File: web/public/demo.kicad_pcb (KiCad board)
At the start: 2 copper layers, 50 x 30 mm, 1 part

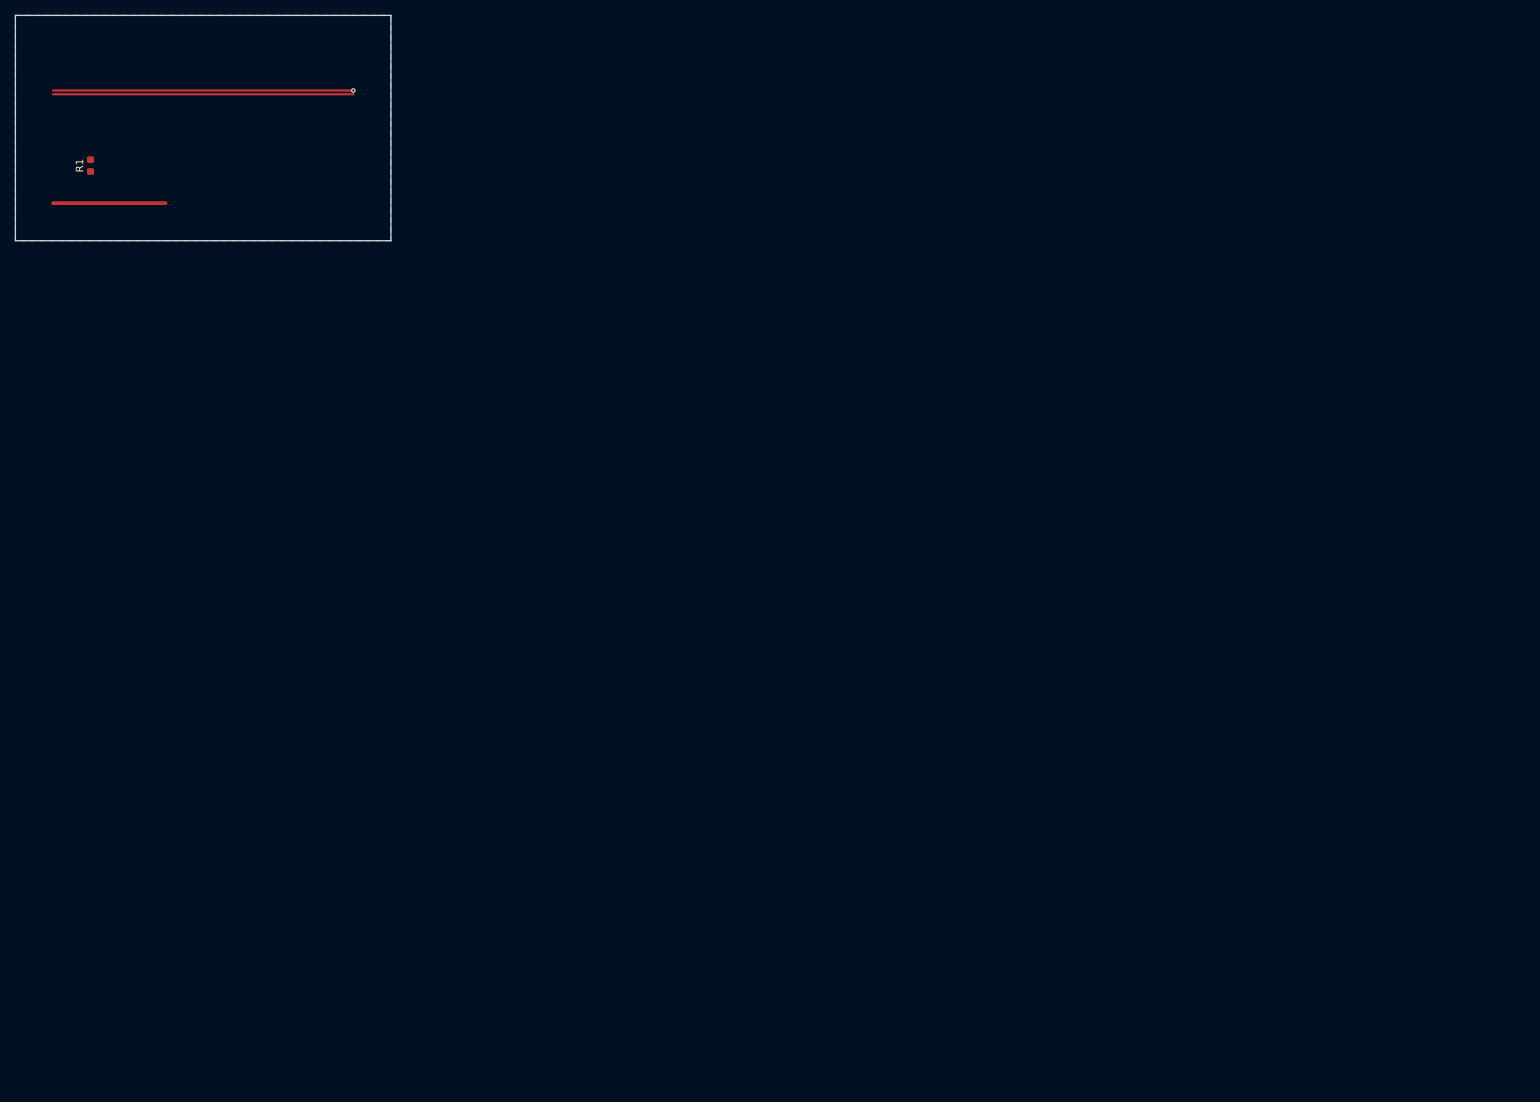
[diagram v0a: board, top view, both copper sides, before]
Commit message: The demo board is now a real converter: LibreSolar MPPT 2420 HC
The served demo was a 2 kB synthetic two-trace board — it demonstrated
coupled-run and nothing Faraday is actually FOR. It is now the
LibreSolar MPPT 2420 HC (CERN-OHL-W-2.0, already attributed in
fixtures/real/ATTRIBUTION.md): a real 20 A synchronous buck that shows
switch nodes, the DERIVED commutation loop (Q1+Q2+C3 by
current-switching analysis), the assumed-stackup flow (KiCad 5 file,
no stackup), return-path breaks, the near-field map and the emissions
panel. The chip names it and carries the license in its tooltip.

The old tiny board still had a job — the stitching fix's
honest-refusal path (no reference via to copy a style from) — so it
moved inline into the returnpath spec instead of being served.

Co-Authored-By: Claude Opus 5 (1M context) <noreply@anthropic.com>
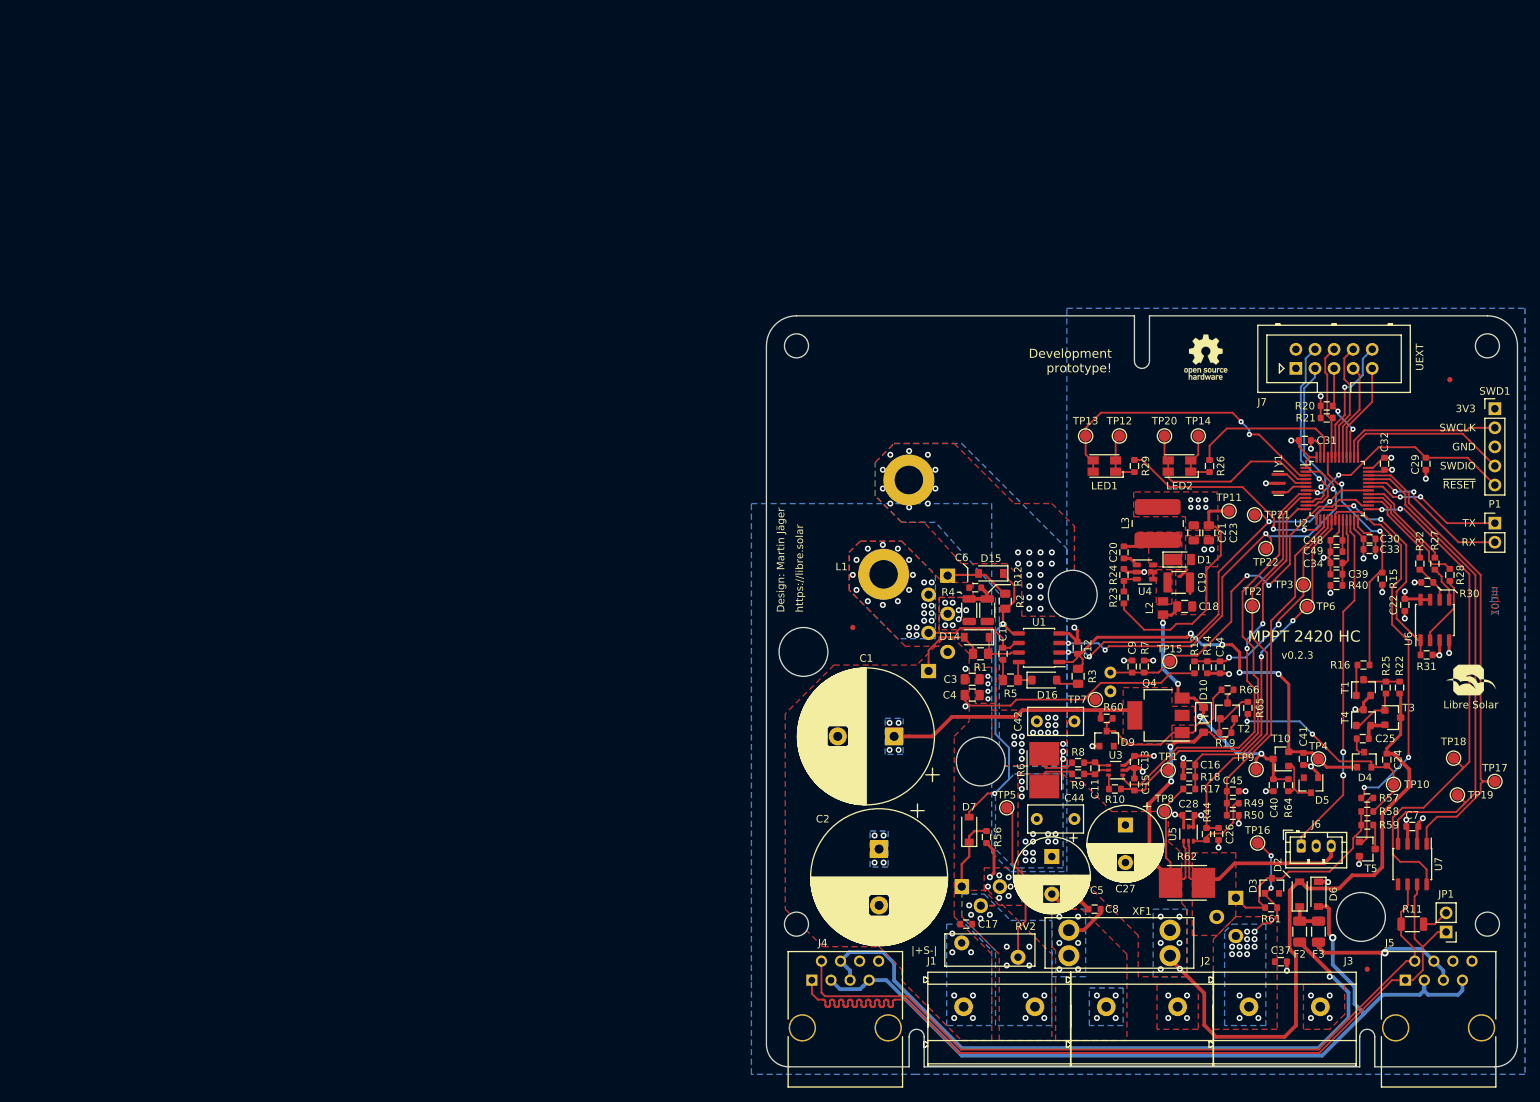
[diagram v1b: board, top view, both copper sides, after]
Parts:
- added C1: 390µF, Capacitor_THT:CP_Radial_D18.0mm_P7.50mm, F.Cu at (117.0, 96.0)
- added C10: 100nF, LibreSolar:C_0603_1608, F.Cu at (131.5, 85.0)
- added C11: 1nF, LibreSolar:C_0603_1608, F.Cu at (143.8, 100.2)
- added C12: 2.2µF, LibreSolar:C_0603_1608, F.Cu at (141.4, 84.2)
- added C13: 100nF, LibreSolar:C_0603_1608, F.Cu at (149.0, 99.4)
- added C14: 10nF, LibreSolar:C_0603_1608, F.Cu at (160.4, 86.8)
- added C15: 1nF, LibreSolar:C_0603_1608, F.Cu at (149.0, 102.4)
- added C16: 10nF, LibreSolar:C_0603_1608, F.Cu at (156.3, 99.8)
- added C17: 10nF, LibreSolar:C_0603_1608, F.Cu at (126.6, 121.0)
- added C18: 1µF, LibreSolar:C_0805_2012, F.Cu at (155.7, 78.7)
- added C19: 4.7µF, LibreSolar:C_1210_3225, F.Cu at (154.9, 75.5)
- added C2: 390µF, Capacitor_THT:CP_Radial_D18.0mm_P7.50mm, F.Cu at (115.0, 111.0)
- added C20: 100nF, LibreSolar:C_0603_1608, F.Cu at (147.6, 71.5)
- added C21: 10µF, LibreSolar:C_0805_2012, F.Cu at (156.9, 68.9)
- added C22: 100nF, LibreSolar:C_0603_1608, F.Cu at (185.0, 78.5)
- added C23: 10µF, LibreSolar:C_0805_2012, F.Cu at (158.9, 68.9)
- added C24: 100nF, LibreSolar:C_0603_1608, F.Cu at (182.6, 99.1)
- added C25: 10nF, LibreSolar:C_0603_1608, F.Cu at (179.4, 96.3)
- added C26: 10nF, LibreSolar:C_0603_1608, F.Cu at (160.2, 109.0)
- added C27: 680µF, Capacitor_THT:CP_Radial_D10.0mm_P5.00mm, F.Cu at (147.8, 107.8)
- added C28: 100nF, LibreSolar:C_0603_1608, F.Cu at (156.2, 106.5)
- added C29: 100nF, LibreSolar:C_0603_1608, F.Cu at (187.8, 59.7)
- added C3: 1µF, LibreSolar:C_0805_2012, F.Cu at (127.4, 88.4)
- added C30: 100nF, LibreSolar:C_0603_1608, F.Cu at (180.3, 69.7)
- added C31: 100nF, LibreSolar:C_0603_1608, F.Cu at (171.7, 56.6)
- added C32: 100nF, LibreSolar:C_0603_1608, F.Cu at (182.3, 59.7)
- added C33: 2.2µF, LibreSolar:C_0603_1608, F.Cu at (180.3, 71.1)
- added C34: 10nF, LibreSolar:C_0603_1608, F.Cu at (175.9, 72.9)
- added C37: 10nF, LibreSolar:C_0603_1608, F.Cu at (168.5, 126.0)
- added C39: 2.2µF, LibreSolar:C_0603_1608, F.Cu at (175.9, 74.4)
- added C4: 100nF, LibreSolar:C_0805_2012, F.Cu at (127.4, 90.5)
- added C40: 1µF, LibreSolar:C_0603_1608, F.Cu at (167.5, 102.5)
- added C41: 4.7µF, LibreSolar:C_0603_1608, F.Cu at (171.5, 99.0)
- added C42: 0.22µF, Capacitor_THT:C_Rect_L7.2mm_W3.5mm_P5.00mm_FKS2_FKP2_MKS2_MKP2, F.Cu at (136.0, 94.0)
- added C44: 0.22µF, Capacitor_THT:C_Rect_L7.2mm_W3.5mm_P5.00mm_FKS2_FKP2_MKS2_MKP2, F.Cu at (141.0, 107.0)
- added C45: 10nF, LibreSolar:C_0603_1608, F.Cu at (162.1, 103.3)
- added C48: 100nF, LibreSolar:C_0603_1608, F.Cu at (175.9, 69.9)
- added C49: 2.2µF, LibreSolar:C_0603_1608, F.Cu at (175.9, 71.4)
- added C5: 680µF, Capacitor_THT:CP_Radial_D10.0mm_P5.00mm, F.Cu at (138.0, 112.0)
- added C6: 2.2nF, LibreSolar:C_0603_1608, F.Cu at (127.8, 76.2)
- added C7: 100nF, LibreSolar:C_0603_1608, F.Cu at (186.0, 108.0)
- added C8: 10nF, LibreSolar:C_0603_1608, F.Cu at (143.7, 119.0)
- added C9: 100nF, LibreSolar:C_0603_1608, F.Cu at (148.7, 86.7)
- added D1: SS16FP, Diode_SMD:D_PowerDI-123, F.Cu at (155.0, 72.5)
- added D10: 1N4148, LibreSolar:D_SOD-123, F.Cu at (158.2, 93.8)
- added D14: SS14FL, Diode_SMD:D_SOD-123, F.Cu at (128.0, 82.8)
- added D15: SS14FL, Diode_SMD:D_SOD-123, F.Cu at (129.9, 74.3)
- added D16: 1N4148, LibreSolar:D_SOD-123, F.Cu at (137.0, 88.5)
- added D2: NRVTS260ESFT1G, Diode_SMD:D_SOD-123, F.Cu at (171.0, 117.0)
- added D3: 12V, Diode_SMD:D_SOT-23_ANK, F.Cu at (167.3, 115.9)
- added D4: BAS70-04, Package_TO_SOT_SMD:SOT-23, F.Cu at (179.6, 99.1)
- added D5: 12V, Diode_SMD:D_SOT-23_ANK, F.Cu at (172.5, 102.5)
- added D6: NRVTS260ESFT1G, Diode_SMD:D_SOD-123, F.Cu at (173.5, 117.0)
- added D7: SS14FL, Diode_SMD:D_SOD-123, F.Cu at (127.0, 108.4)
- added D9: 47V, Diode_SMD:D_SOT-23_ANK, F.Cu at (145.3, 96.3)
- added F1: 25A, LibreSolar:NULL, F.Cu at (147.0, 123.5)
- added F2: 500mA, Fuse:Fuse_1206_3216Metric, F.Cu at (171.0, 122.0)
- added F3: 500mA, Fuse:Fuse_1206_3216Metric, F.Cu at (173.5, 122.0)
- added FID1: Fiducial, LibreSolar:Fiducial_0.7mm, F.Cu at (180.0, 127.0)
- added FID2: Fiducial, LibreSolar:Fiducial_0.7mm, F.Cu at (111.5, 81.5)
- added FID3: Fiducial, LibreSolar:Fiducial_0.7mm, F.Cu at (191.0, 48.5)
- added J1: MKDS 5/ 2-9,5, LibreSolar:Phoenix_Contact_MKDS_5-2-9,5, F.Cu at (126.2, 132.0)
- added J2: MKDS 5/ 2-9,5, LibreSolar:Phoenix_Contact_MKDS_5-2-9,5, F.Cu at (145.2, 132.0)
- added J3: MKDS 5/ 2-9,5, LibreSolar:Phoenix_Contact_MKDS_5-2-9,5, F.Cu at (164.2, 132.0)
- added J4: 8P8C, LibreSolar:RJ45_8P8C, F.Cu at (110.5, 131.0)
- added J5: 8P8C, LibreSolar:RJ45_8P8C, F.Cu at (189.5, 131.0)
- added J6: JST PH, Connector_JST:JST_PH_B3B-PH-K_1x03_P2.00mm_Vertical, F.Cu at (171.2, 110.6)
- added J7: UEXT, LibreSolar:Box_Header_2x05x2.54mm_Straight, F.Cu at (170.5, 47.0)
- added JP1: Jumper_NC_Small, Connector_PinHeader_2.54mm:PinHeader_1x02_P2.54mm_Vertical, F.Cu at (190.5, 122.0)
- added L1: 53µH, LibreSolar:Inductor_Toroid_D32.8mm_4mm2, F.Cu at (120.0, 58.0)
- added L2: 4.7µH, Inductor_SMD:L_0805_2012Metric, F.Cu at (152.8, 78.9)
- added L3: 47µH, LibreSolar:Bourns_SRN6045TA, F.Cu at (152.1, 67.7)
- added LED1: LED_Dual_PLCC4, LED_SMD:LED_Avago_PLCC4_3.2x2.8mm_CW, F.Cu at (145.0, 60.0)
- added LED2: LED_Dual_PLCC4, LED_SMD:LED_Avago_PLCC4_3.2x2.8mm_CW, F.Cu at (155.0, 60.0)
- added LOGO1: LIBRE_SOLAR, LibreSolar:LIBRESOLAR_LOGO, F.Cu at (191.5, 90.5)
- added LOGO2: OPEN_HARDWARE, Symbol:OSHW-Logo_5.7x6mm_SilkScreen, F.Cu at (158.5, 45.5)
- added MK1: Mounting_Hole, MountingHole:MountingHole_3.2mm_M3, F.Cu at (104.0, 121.0)
- added MK2: Mounting_Hole, MountingHole:MountingHole_3.2mm_M3, F.Cu at (196.0, 121.0)
- added MK3: Mounting_Hole, MountingHole:MountingHole_3.2mm_M3, F.Cu at (196.0, 44.0)
- added MK4: Mounting_Hole, MountingHole:MountingHole_3.2mm_M3, F.Cu at (104.0, 44.0)
- added P1: CONN_01X02, Connector_PinHeader_2.54mm:PinHeader_1x02_P2.54mm_Vertical, F.Cu at (197.0, 67.6)
- added Q1: IPA045N10N3G, LibreSolar:TO-220-3_Horizontal_BottomHeatsink, B.Cu at (121.6, 87.3)
- added Q2: IPA045N10N3G, LibreSolar:TO-220-3_Horizontal_BottomHeatsink, B.Cu at (124.1, 74.6)
- added Q3: IPA045N10N3G, LibreSolar:TO-220-3_Horizontal_BottomHeatsink, B.Cu at (126.0, 116.0)
- added Q4: BUK98180-100A, Package_TO_SOT_SMD:SOT-223-3_TabPin2, F.Cu at (152.2, 93.2)
- added Q7: IPA045N10N3G, LibreSolar:TO-220-3_Horizontal_BottomHeatsink, B.Cu at (162.5, 117.5)
- added R10: 1k, LibreSolar:R_0603_1608, F.Cu at (146.4, 103.0)
- added R11: 120R, LibreSolar:R_1206_3216, F.Cu at (186.0, 121.0)
- added R12: 4R7, LibreSolar:R_1206_3216, F.Cu at (129.4, 79.2)
- added R13: 100k, LibreSolar:R_0603_1608, F.Cu at (157.0, 86.8)
- added R14: 2.2k, LibreSolar:R_0603_1608, F.Cu at (158.7, 86.8)
- added R15: 1M, LibreSolar:R_0603_1608, F.Cu at (182.0, 75.0)
- added R16: 10k, LibreSolar:R_0603_1608, F.Cu at (179.5, 86.5)
- added R17: 100k, LibreSolar:R_0603_1608, F.Cu at (156.3, 103.0)
- added R18: 5.6k, LibreSolar:R_0603_1608, F.Cu at (156.3, 101.4)
- added R19: 10k, LibreSolar:R_0603_1608, F.Cu at (161.1, 95.5)
- added R2: 3R3, LibreSolar:R_0805_2012, F.Cu at (131.8, 78.0)
- added R20: 2.2k, LibreSolar:R_0603_1608, F.Cu at (174.6, 52.0)
- added R21: 2.2k, LibreSolar:R_0603_1608, F.Cu at (174.6, 53.6)
- added R22: 100k, LibreSolar:R_0603_1608, F.Cu at (184.3, 89.5)
- added R23: 33k, LibreSolar:R_0603_1608, F.Cu at (147.6, 77.5)
- added R24: 10k, LibreSolar:R_0603_1608, F.Cu at (147.6, 74.5)
- added R25: 1k, LibreSolar:R_0603_1608, F.Cu at (182.5, 89.5)
- added R26: 1k, LibreSolar:R_0603_1608, F.Cu at (159.0, 60.0)
- added R27: 47R, LibreSolar:R_0603_1608, F.Cu at (189.0, 73.0)
- added R28: 47R, LibreSolar:R_0603_1608, F.Cu at (191.0, 74.5)
- added R29: 1k, LibreSolar:R_0603_1608, F.Cu at (149.0, 60.0)
- added R3: 3R3, LibreSolar:R_0805_2012, F.Cu at (141.5, 88.0)
- added R30: 100k, LibreSolar:R_0603_1608, F.Cu at (188.0, 75.5)
- added R31: 2.2k, LibreSolar:R_0603_1608, F.Cu at (187.9, 85.2)
- added R32: 47R, LibreSolar:R_0603_1608, F.Cu at (187.0, 73.0)
- added R4: 4R7, LibreSolar:R_1206_3216, F.Cu at (127.0, 79.2)
- added R40: 47R, LibreSolar:R_0603_1608, F.Cu at (175.9, 75.9)
- added R44: 2.2k, LibreSolar:R_0603_1608, F.Cu at (158.6, 109.0)
- added R49: 10k, LibreSolar:R_0603_1608, F.Cu at (162.1, 104.9)
- added R5: 3R3, LibreSolar:R_0805_2012, F.Cu at (132.5, 88.5)
- added R50: 8.2k, LibreSolar:C_0603_1608, F.Cu at (162.1, 106.5)
- added R56: 1M, LibreSolar:R_0603_1608, F.Cu at (129.3, 109.4)
- added R57: 2.2k, LibreSolar:R_0603_1608, F.Cu at (180.0, 104.2)
- added R58: 100k, LibreSolar:R_0603_1608, F.Cu at (180.0, 106.0)
- added R59: 10k, LibreSolar:R_0603_1608, F.Cu at (180.0, 107.8)
- added R6: 2m, LibreSolar:R_Bourns_CRE2512, F.Cu at (137.0, 100.5)
- added R60: 100k, LibreSolar:R_0603_1608, F.Cu at (145.3, 93.6)
- added R61: 1M, LibreSolar:R_0603_1608, F.Cu at (167.2, 118.8)
- added R62: 2m, LibreSolar:R_Bourns_CRE2512, F.Cu at (156.0, 115.5)
- added R64: 10k, LibreSolar:R_0603_1608, F.Cu at (169.5, 102.5)
- added R65: 100k, LibreSolar:R_0603_1608, F.Cu at (164.1, 92.2)
- added R66: 1k, LibreSolar:R_0603_1608, F.Cu at (161.4, 89.8)
- added R7: 10k, LibreSolar:R_0603_1608, F.Cu at (150.3, 86.7)
- added R8: 10R, LibreSolar:R_0603_1608, F.Cu at (141.5, 99.5)
- added R9: 10R, LibreSolar:R_0603_1608, F.Cu at (141.5, 101.0)
- added RT1: 10k, Capacitor_THT:C_Disc_D3.8mm_W2.6mm_P2.50mm, B.Cu at (145.8, 87.5)
- added RV2: 82V, Varistor:RV_Disc_D12mm_W4.3mm_P7.5mm, F.Cu at (126.0, 123.5)
- added SWD1: ST_Nucleo_SWD, Connector_PinHeader_2.54mm:PinHeader_1x05_P2.54mm_Vertical, F.Cu at (197.0, 52.4)
- added T1: BC846B, LibreSolar:SOT-23, F.Cu at (179.5, 89.5)
- added T10: BC846B, LibreSolar:SOT-23, F.Cu at (168.5, 99.0)
- added T2: BC846B, LibreSolar:SOT-23, F.Cu at (161.4, 92.6)
- added T3: BC846B, LibreSolar:SOT-23, F.Cu at (183.4, 93.5)
- added T4: BC856B, LibreSolar:SOT-23, F.Cu at (179.5, 93.5)
- added T5: BC846B, LibreSolar:SOT-23, F.Cu at (180.0, 111.0)
- added TP1: 1.5mm, TestPoint:TestPoint_Pad_D1.5mm, F.Cu at (153.5, 100.5)
- added TP10: 1.5mm, TestPoint:TestPoint_Pad_D1.5mm, F.Cu at (183.5, 102.4)
- added TP11: 1.5mm, TestPoint:TestPoint_Pad_D1.5mm, F.Cu at (161.6, 66.0)
- added TP12: 1.5mm, TestPoint:TestPoint_Pad_D1.5mm, F.Cu at (147.0, 56.0)
- added TP13: 1.5mm, TestPoint:TestPoint_Pad_D1.5mm, F.Cu at (142.5, 56.0)
- added TP14: 1.5mm, TestPoint:TestPoint_Pad_D1.5mm, F.Cu at (157.5, 56.0)
- added TP15: 1.5mm, TestPoint:TestPoint_Pad_D1.5mm, F.Cu at (153.7, 86.0)
- added TP16: 1.5mm, TestPoint:TestPoint_Pad_D1.5mm, F.Cu at (165.4, 110.2)
- added TP17: 1.5mm, TestPoint:TestPoint_Pad_D1.5mm, F.Cu at (197.0, 102.0)
- added TP18: 1.5mm, TestPoint:TestPoint_Pad_D1.5mm, F.Cu at (191.5, 98.9)
- added TP19: 1.5mm, TestPoint:TestPoint_Pad_D1.5mm, F.Cu at (192.0, 103.8)
- added TP2: 1.5mm, TestPoint:TestPoint_Pad_D1.5mm, F.Cu at (164.7, 78.6)
- added TP20: 1.5mm, TestPoint:TestPoint_Pad_D1.5mm, F.Cu at (153.0, 56.0)
- added TP21: 1.5mm, TestPoint:TestPoint_Pad_D1.5mm, F.Cu at (165.0, 66.5)
- added TP22: 1.5mm, TestPoint:TestPoint_Pad_D1.5mm, F.Cu at (166.5, 71.0)
- added TP3: 1.5mm, TestPoint:TestPoint_Pad_D1.5mm, F.Cu at (171.5, 75.8)
- added TP4: 1.5mm, TestPoint:TestPoint_Pad_D1.5mm, F.Cu at (173.5, 99.0)
- added TP5: 1.5mm, TestPoint:TestPoint_Pad_D1.5mm, F.Cu at (132.0, 105.5)
- added TP6: 1.5mm, TestPoint:TestPoint_Pad_D1.5mm, F.Cu at (172.0, 78.7)
- added TP7: 1.5mm, TestPoint:TestPoint_Pad_D1.5mm, F.Cu at (143.8, 91.1)
- added TP8: 1.5mm, TestPoint:TestPoint_Pad_D1.5mm, F.Cu at (153.0, 106.0)
- added TP9: 1.5mm, TestPoint:TestPoint_Pad_D1.5mm, F.Cu at (165.2, 100.4)
- added U1: LM5107, LibreSolar:SOIC-8_3.9x4.9mm_Pitch1.27mm, F.Cu at (136.3, 84.2)
- added U2: STM32G431CBTx, Package_QFP:LQFP-48_7x7mm_P0.5mm, F.Cu at (176.0, 63.0)
- added U3: INA186, Package_TO_SOT_SMD:SOT-363_SC-70-6, F.Cu at (146.5, 100.5)
- added U4: LMR16006X, LibreSolar:SOT-23-6, F.Cu at (150.4, 74.1)
- added U5: INA186, Package_TO_SOT_SMD:SOT-363_SC-70-6, F.Cu at (156.2, 109.0)
- added U6: W25Q80DVS, LibreSolar:SOIC-8_3.9x4.9mm_Pitch1.27mm, F.Cu at (189.0, 80.5)
- added U7: TCAN334, LibreSolar:SOIC-8_3.9x4.9mm_Pitch1.27mm, F.Cu at (186.0, 113.0)
- added XF1: Fuse_Holder, LibreSolar:Keystone-Fuse-3557-2, F.Cu at (147.0, 123.5)
- added Y1: 8MHz, LibreSolar:Resonator_Murata_CSTNE, F.Cu at (168.2, 62.3)
- R1: value 100n -> 3R3; footprint Resistor_SMD:R_0603_1608Metric -> LibreSolar:R_0805_2012
- moved R1 135.2 mm to (128.5, 85.0), turned to 0 degrees
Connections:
- R1 pad 1: CLK -> Net-(D14-Pad2)
- R1 pad 2: GND -> /DC/DC/HS_DRV
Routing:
- net VBUS: track 0.00 -> 142.2 mm, vias 0 -> 22
- net /CAN_H: track 0.00 -> 118.8 mm
- net /CAN_GND: track 0.00 -> 114.9 mm, vias 0 -> 1
- net /CAN_L: track 0.00 -> 102.6 mm
- net /CAN/CAN_PWR1: track 0.00 -> 92.6 mm, vias 0 -> 1
- net +3V3: track 0.00 -> 71.5 mm, vias 0 -> 17
- net /DCDC_HV+: track 0.00 -> 69.7 mm, vias 0 -> 17
- net /CAN/CAN_STB: track 0.00 -> 69.7 mm, vias 0 -> 2
- net GND: track 15.0 -> 82.7 mm, vias 0 -> 64
- net /CAN/CAN_RX: track 0.00 -> 66.1 mm
- net /CAN/CAN_TX: track 0.00 -> 63.3 mm
- net /MCU/ADC12_IN1: track 0.00 -> 59.2 mm
- net /DC/DC/PWM_LS: track 0.00 -> 58.7 mm, vias 0 -> 4
- net +12V: track 0.00 -> 58.4 mm, vias 0 -> 4
- net /DC/DC/PWM_HS: track 0.00 -> 56.3 mm, vias 0 -> 4
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- added copper zone on 3V3, net +3V3
- added copper zone on F.Cu, net +3V3
- added copper zone on B.Cu, net /BAT+
- added copper zone on F.Cu, net /BAT+
- added copper zone on 3V3, net /DC/DC/SHUNT_DCDC_P
- added copper zone on B.Cu, net /DC/DC/SHUNT_DCDC_P
- added copper zone on F.Cu, net /DC/DC/SHUNT_DCDC_P
- added copper zone on 3V3, net /DC/DC/SW_NODE
- added copper zone on B.Cu, net /DC/DC/SW_NODE
- added copper zone on F.Cu, net /DC/DC/SW_NODE
- added copper zone on GND, net /DC/DC/SW_NODE
- added copper zone on 3V3, net /DCDC_HV+
- added copper zone on B.Cu, net /DCDC_HV+
- added copper zone on F.Cu, net /DCDC_HV+
- added copper zone on B.Cu, net /DCDC_HV-
- added copper zone on F.Cu, net /DCDC_HV-
- added copper zone on B.Cu, net /LOAD+
- added copper zone on F.Cu, net /LOAD+
- added copper zone on F.Cu, net /MEAS_LV+
- added copper zone on F.Cu, net GND
- added copper zone on GND, net GND
- added copper zone on F.Cu, net Net-(C19-Pad1)
- added copper zone on F.Cu, net Net-(C20-Pad2)
- added copper zone on B.Cu, net VBUS
- added copper zone on F.Cu, net VBUS
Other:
- board size 50 x 30 mm -> 100 x 100 mm
- copper layers 2 -> 4
- net class Default added: clearance 0.2, trace_width 0.25, via_dia 0.7, via_drill 0.3
- net class Power added: clearance 0.2, trace_width 0.4, via_dia 0.8, via_drill 0.4
- board text added: "35µm"
- board text added: "3V3"
- board text added: "4-layer PCB Inner layers: 35 µm copper Outer layers: 70 µm copper Silk-screen on both sides"
- board text added: "70µm"
- board text added: "Design: Martin Jäger"
- board text added: "Development prototype!"
- board text added: "GND"
- board text added: "MISO"
- board text added: "MOSI"
- board text added: "MPPT 2420 HC"
- board text added: "RX"
- board text added: "SCK"
- board text added: "SCL"
- board text added: "SDA"
- board text added: "SSEL"
- board text added: "SWCLK"
- board text added: "SWDIO"
- board text added: "TX"
- board text added: "UEXT"
- board text added: "https://libre.solar"
- board text added: "v0.2.3"
- board text added: "|+S-|"
- board text added: "~RESET"
